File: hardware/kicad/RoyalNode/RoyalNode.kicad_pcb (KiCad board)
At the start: 4 copper layers, 85 x 75 mm, 69 parts, among them J1 XT30PW-M C431092 RC, J2 XT30PW-M C431092 RC, J3 J_LOW_JST_GH_SM02B_GHS_TB_RC, J4 J_LOW_JST_GH_SM02B_GHS_TB_RC, J5 SMA edge envelope, J6 J_LOW_JST_GH_SM04B_GHS_TB_RC, Q1 Infineon PG-DSO-8-27 thermal 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, Q2 Infineon PG-DSO-8-27 thermal 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, Q3 Infineon PG-DSO-8-27 thermal 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, U1 BQ25798 RQM0029A RC, U2 LM66100 DCK0006A SC70-6 RC, U3 TPS61088 RHL0020A thermal via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, U4 LTC4365 TSOT-23-8 RC

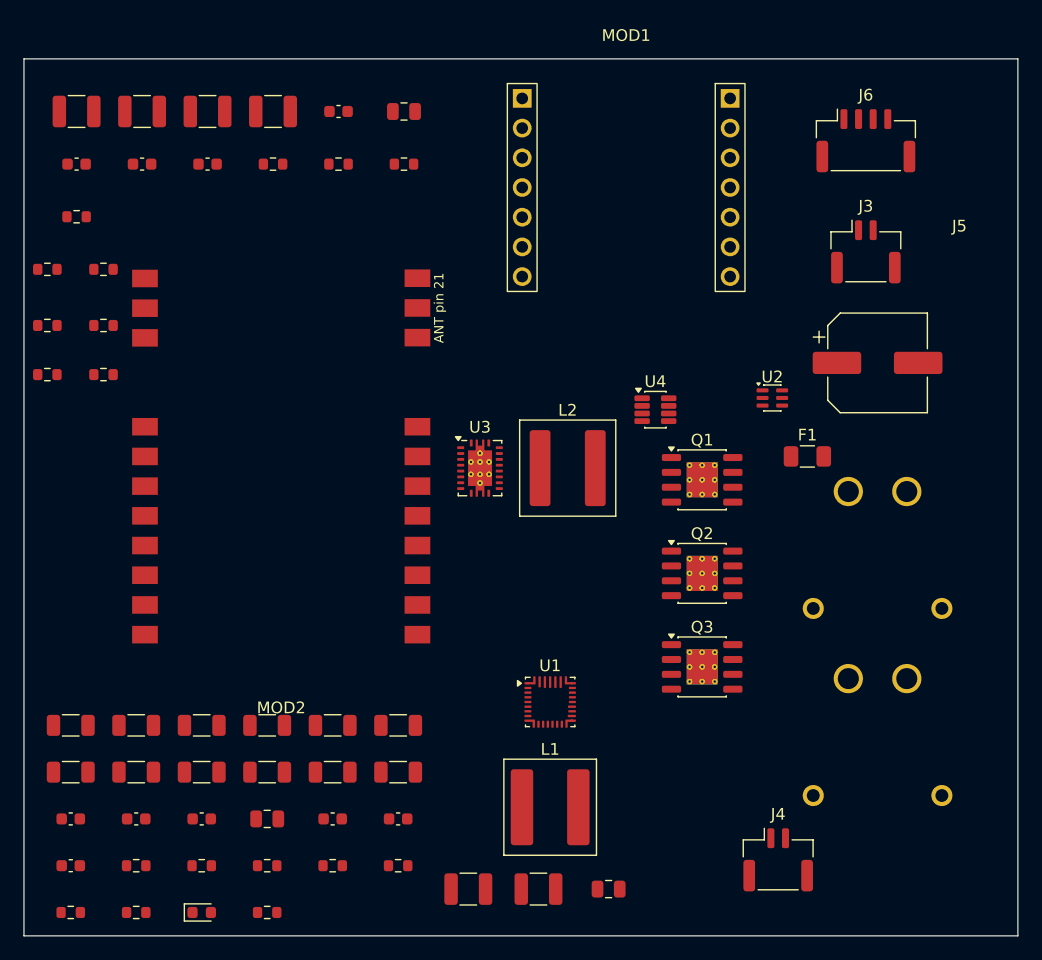
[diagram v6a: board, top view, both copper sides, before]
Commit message: Route initial low-current nets
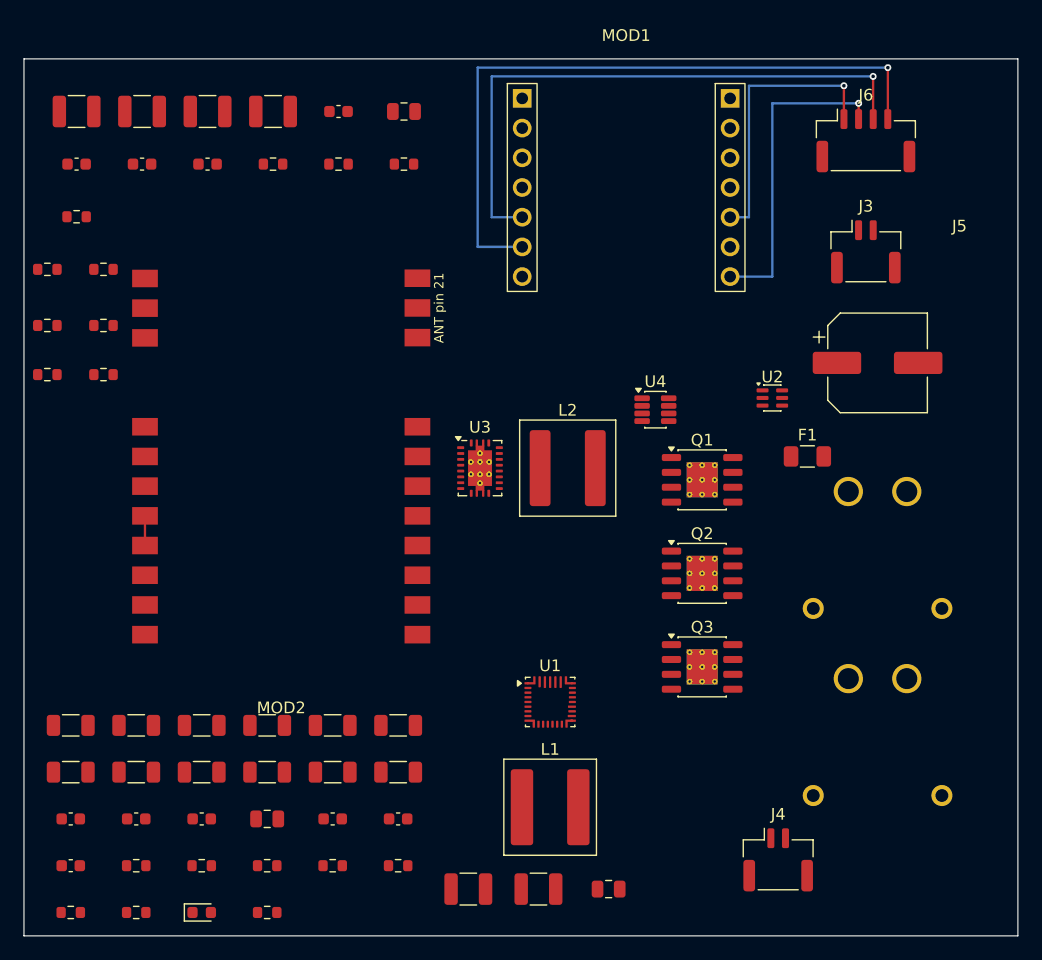
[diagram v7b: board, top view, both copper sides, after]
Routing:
- net I2C_SCL: track 0.00 -> 58.6 mm, vias 0 -> 1
- net I2C_SDA: track 0.00 -> 50.9 mm, vias 0 -> 1
- net GND: track 0.00 -> 27.2 mm, vias 0 -> 1
- net 3V3: track 0.00 -> 23.8 mm, vias 0 -> 1
- net E22_TXEN_DIO2: track 0.00 -> 2.54 mm
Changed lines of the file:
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@@
   	)
   )
+  (segment
+    (start 30.35 59.08)
+    (end 30.35 61.62)
+    (width 0.20)
+    (layer "F.Cu")
+    (net 44)
+  )
+  (segment
+    (start 90.12 25.15)
+    (end 90.12 22.30)
+    (width 0.20)
+    (layer "F.Cu")
+    (net 2)
+  )
+  (segment
+    (start 90.12 22.30)
+    (end 82.00 22.30)
+    (width 0.20)
+    (layer "B.Cu")
+    (net 2)
+  )
+  (segment
+    (start 82.00 22.30)
+    (end 82.00 33.54)
+    (width 0.20)
+    (layer "B.Cu")
+    (net 2)
+  )
+  (segment
+    (start 82.00 33.54)
+    (end 80.39 33.54)
+    (width 0.20)
+    (layer "B.Cu")
+    (net 2)
+  )
+  (segment
+    (start 91.38 25.15)
+    (end 91.38 23.80)
+    (width 0.20)
+    (layer "F.Cu")
+    (net 1)
+  )
+  (segment
+    (start 91.38 23.80)
+    (end 84.00 23.80)
+    (width 0.20)
+    (layer "B.Cu")
+    (net 1)
+  )
+  (segment
+    (start 84.00 23.80)
+    (end 84.00 38.62)
+    (width 0.20)
+    (layer "B.Cu")
+    (net 1)
+  )
+  (segment
+    (start 84.00 38.62)
+    (end 80.39 38.62)
+    (width 0.20)
+    (layer "B.Cu")
+    (net 1)
+  )
+  (segment
+    (start 92.62 25.15)
+    (end 92.62 21.50)
+    (width 0.20)
+    (layer "F.Cu")
+    (net 46)
+  )
+  (segment
+    (start 92.62 21.50)
+    (end 60.00 21.50)
+    (width 0.20)
+    (layer "B.Cu")
+    (net 46)
+  )
+  (segment
+    (start 60.00 21.50)
+    (end 60.00 33.54)
+    (width 0.20)
+    (layer "B.Cu")
+    (net 46)
+  )
+  (segment
+    (start 60.00 33.54)
+    (end 62.61 33.54)
+    (width 0.20)
+    (layer "B.Cu")
+    (net 46)
+  )
+  (segment
+    (start 93.88 25.15)
+    (end 93.88 20.75)
+    (width 0.20)
+    (layer "F.Cu")
+    (net 45)
+  )
+  (segment
+    (start 93.88 20.75)
+    (end 58.80 20.75)
+    (width 0.20)
+    (layer "B.Cu")
+    (net 45)
+  )
+  (segment
+    (start 58.80 20.75)
+    (end 58.80 36.08)
+    (width 0.20)
+    (layer "B.Cu")
+    (net 45)
+  )
+  (segment
+    (start 58.80 36.08)
+    (end 62.61 36.08)
+    (width 0.20)
+    (layer "B.Cu")
+    (net 45)
+  )
+  (via
+    (at 90.12 22.30)
+    (size 0.60)
+    (drill 0.30)
+    (layers "F.Cu" "B.Cu")
+    (net 2)
+  )
+  (via
+    (at 91.38 23.80)
+    (size 0.60)
+    (drill 0.30)
+    (layers "F.Cu" "B.Cu")
+    (net 1)
+  )
+  (via
+    (at 92.62 21.50)
+    (size 0.60)
+    (drill 0.30)
+    (layers "F.Cu" "B.Cu")
+    (net 46)
+  )
+  (via
+    (at 93.88 20.75)
+    (size 0.60)
+    (drill 0.30)
+    (layers "F.Cu" "B.Cu")
+    (net 45)
+  )
 )

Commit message: Add L2 ground reference plane
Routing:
- added copper zone on In1.Cu, net GND
